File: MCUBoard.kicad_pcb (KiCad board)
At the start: 2 copper layers, 90 x 90 mm, 61 parts, among them J1 USB_B_Micro, J2 Conn_01x04, J3 Conn_02x03_Odd_Even, J4 Conn_02x05_Odd_Even, J5 Conn_01x04, J6 Conn_01x04, J7 Conn_01x16, J8 Conn_02x16_Odd_Even, J9 Conn_01x04, Q1 BSS138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

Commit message: change PB headers and route tracks for port B
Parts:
- added J10: Conn_01x04, Connector_PinHeader_2.54mm:PinHeader_1x04_P2.54mm_Vertical, F.Cu at (93.0, 86.3)
- J8: value Conn_02x16_Odd_Even -> Conn_01x18; footprint Connector_PinHeader_2.54mm:PinHeader_2x16_P2.54mm_Vertical -> Connector_PinHeader_2.54mm:PinHeader_1x18_P2.54mm_Vertical
- moved J8 36.9 mm to (137.7, 79.4), turned to 0 degrees
- moved R15 32.5 mm to (128.6, 135.9)
- moved R14 28.1 mm to (123.9, 132.3)
- moved R13 17.6 mm to (111.7, 115.2)
- moved R12 16.4 mm to (110.5, 110.2)
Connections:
- J8 pad 10: /LV0 -> /PB9
- J8 pad 11: /PB5 -> /PB10
- J8 pad 12: /LV1 -> /PB11
- J8 pad 13: /PB6 -> /PB12
- J8 pad 14: /LV2 -> /PB13
- J8 pad 15: /PB7 -> /PB14
- J8 pad 16: /LV3 -> /PB15
- J8 pad 17: /PB8 -> /PD0
- J8 pad 18: Net-(J8-Pad18) -> /PD1
- J8 pad 2: /PD0 -> /PB1
- J8 pad 3: /PB1 -> /BOOT1
- J8 pad 4: /PD1 -> /PB3
- J8 pad 5: /BOOT1 -> /PB4
- J8 pad 6: Net-(J8-Pad6) -> /PB5
- J8 pad 7: /PB3 -> /PB6
- J8 pad 8: Net-(J8-Pad8) -> /PB7
- J8 pad 9: /PB4 -> /PB8
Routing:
- net /PB15: track 0.00 -> 27.1 mm
- net /PB8: track 0.00 -> 25.8 mm, vias 0 -> 2
- net /PB14: track 0.00 -> 25.0 mm
- net /PB11: track 0.00 -> 24.2 mm, vias 0 -> 2
- net /PB0: track 0.00 -> 24.2 mm
- net /PB10: track 0.00 -> 24.0 mm, vias 0 -> 2
- net /PB4: track 0.00 -> 23.1 mm, vias 0 -> 2
- net /PB3: track 0.00 -> 23.0 mm, vias 0 -> 2
- net /PB13: track 0.00 -> 23.0 mm
- net /PB7: track 0.00 -> 22.9 mm, vias 0 -> 2
- net /PB1: track 0.00 -> 22.6 mm
- net /PB6: track 0.00 -> 22.6 mm, vias 0 -> 2
- net /PB9: track 0.00 -> 22.6 mm, vias 0 -> 2
- net /PB5: track 0.00 -> 22.4 mm, vias 0 -> 2
- net /PB12: track 0.00 -> 20.9 mm
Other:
- net class Default: clearance 0.2 -> 0.155; trace_width 0.25 -> 0.155; via_dia 0.8 -> 0.6; via_drill 0.4 -> 0.3
- net class six mil added: clearance 0.155, trace_width 0.155, via_dia 0.8, via_drill 0.4
- rule trace_clearance: 0.2 -> 0.155
- rule trace_min: 0.2 -> 0.155

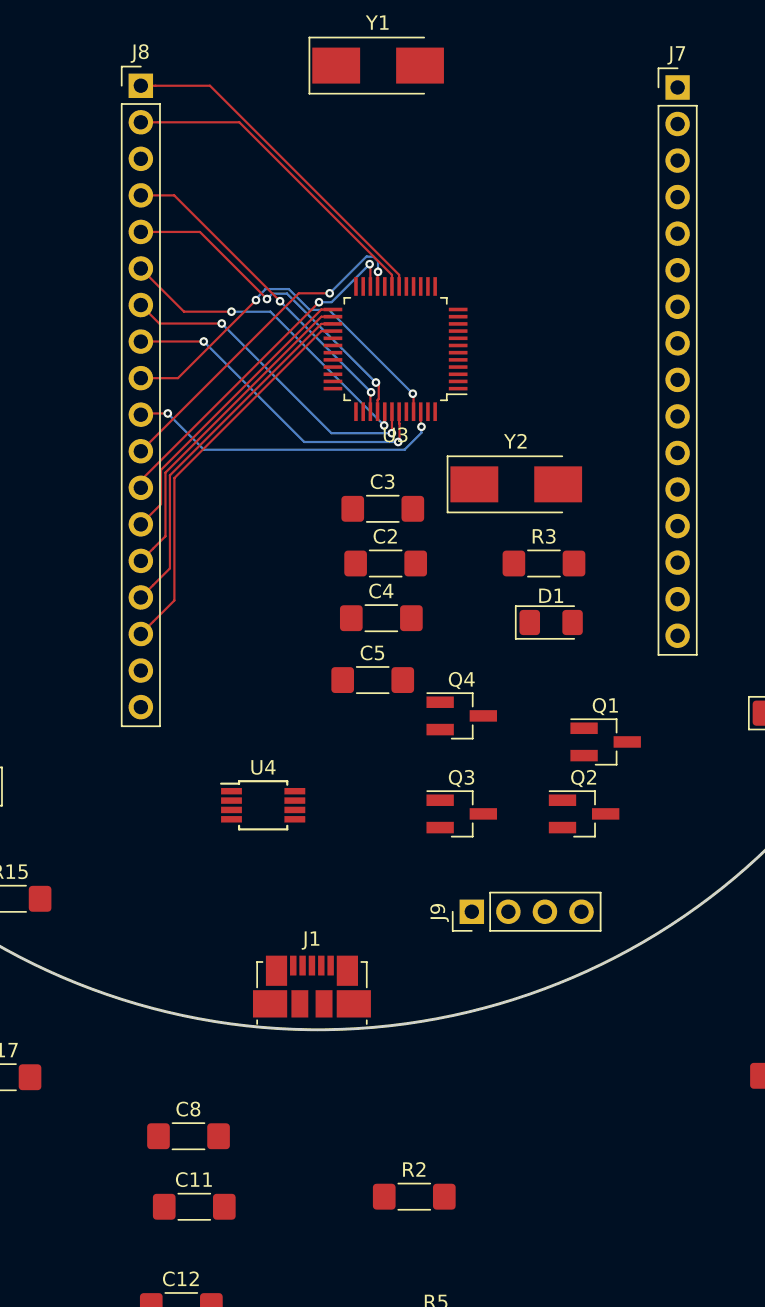
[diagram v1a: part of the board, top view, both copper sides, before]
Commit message: route portA and usb
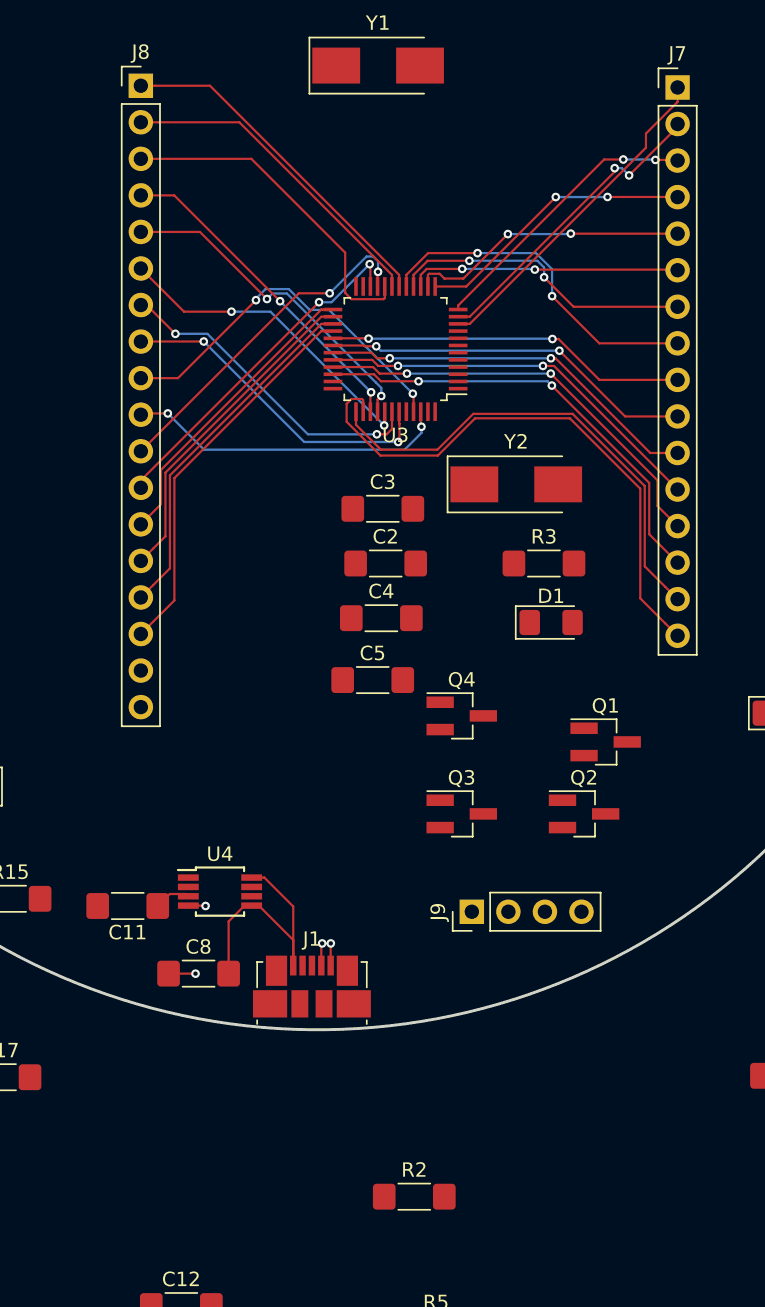
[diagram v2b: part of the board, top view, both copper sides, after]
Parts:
- moved C11 21.4 mm to (136.8, 136.4), turned to 180 degrees
- moved C8 11.3 mm to (141.7, 141.1)
- moved U4 6.71 mm to (143.2, 135.4)
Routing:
- net /PA15: track 0.00 -> 39.1 mm
- net /SWDCLK: track 0.00 -> 33.6 mm
- net /SWDIO: track 0.00 -> 31.5 mm, vias 0 -> 2
- net /PA12: track 0.00 -> 29.6 mm, vias 0 -> 2
- net /PA11: track 0.00 -> 27.7 mm, vias 0 -> 2
- net /PA10: track 0.00 -> 26.8 mm, vias 0 -> 2
- net /PA9: track 0.00 -> 26.0 mm, vias 0 -> 2
- net /PA8: track 0.00 -> 25.1 mm, vias 0 -> 2
- net /PA7: track 0.00 -> 24.0 mm, vias 0 -> 2
- net /BOOT1: track 0.00 -> 23.5 mm
- net /PA0: track 0.00 -> 23.2 mm
- net /PA1: track 0.00 -> 21.5 mm, vias 0 -> 2
- net /PA6: track 0.00 -> 21.3 mm, vias 0 -> 2
- net /PA2: track 0.00 -> 19.8 mm, vias 0 -> 2
- net /PA4: track 0.00 -> 19.6 mm, vias 0 -> 2
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
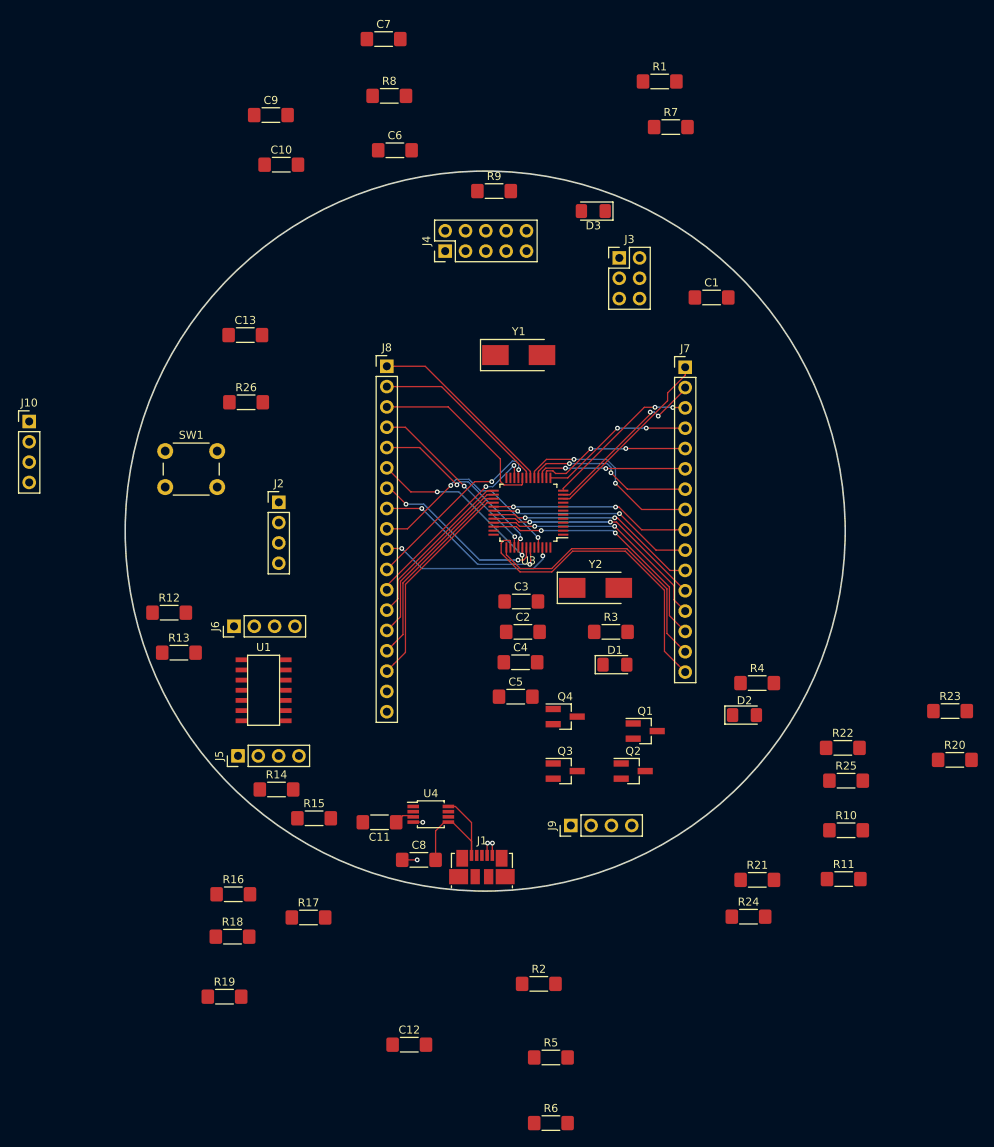
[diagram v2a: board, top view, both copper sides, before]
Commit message: routing bi-directional level shifters
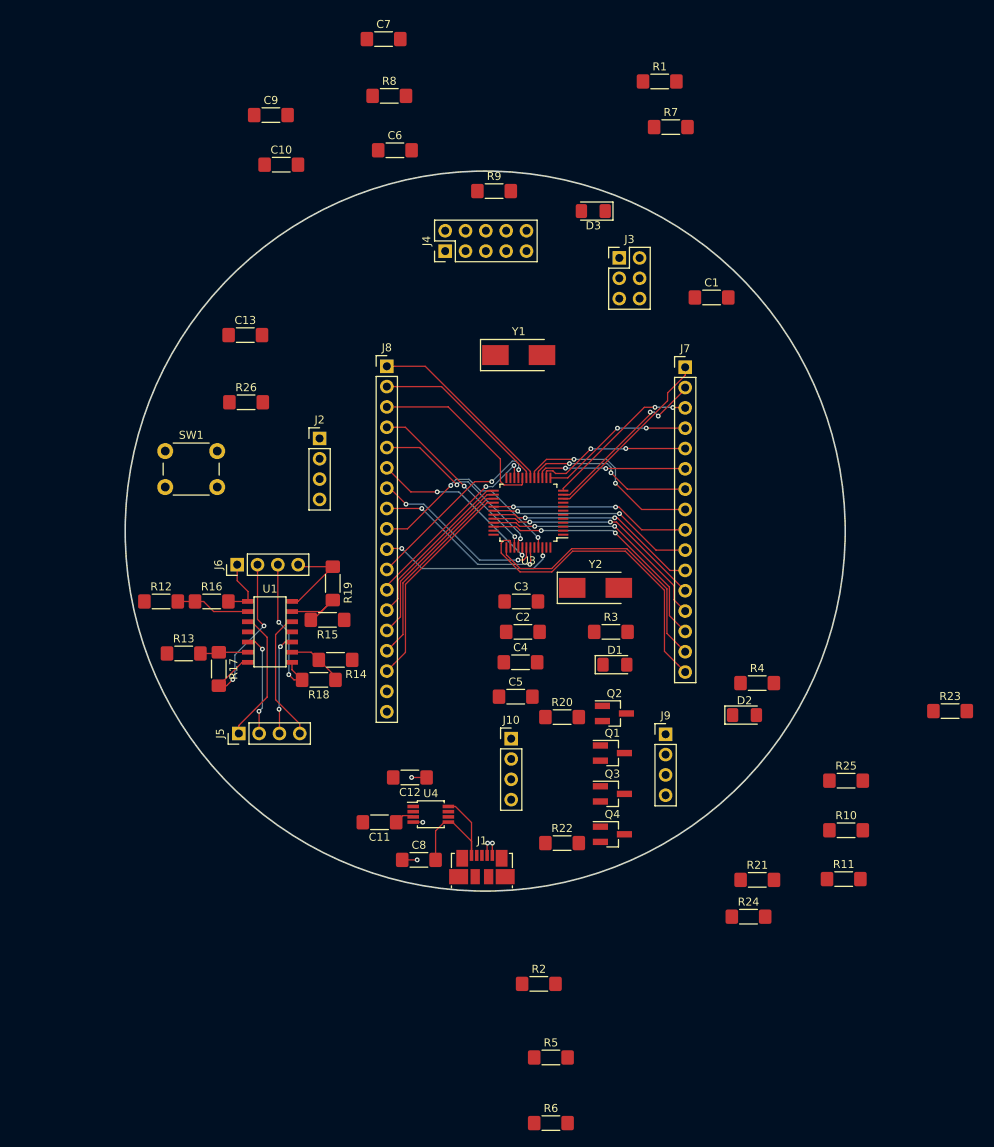
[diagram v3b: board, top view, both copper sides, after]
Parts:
- moved J10 72.1 mm to (153.2, 126.0)
- moved R19 53.4 mm to (130.9, 106.5), turned to 90 degrees
- moved R20 49.4 mm to (159.6, 123.2)
- moved R22 37.1 mm to (159.6, 139.0)
- moved R16 36.7 mm to (115.8, 108.8)
- moved R18 33.9 mm to (129.2, 118.6), turned to 180 degrees
- moved C12 33.4 mm to (140.6, 130.8), turned to 180 degrees
- moved R17 33.0 mm to (116.7, 117.2), turned to 270 degrees
- moved R15 24.9 mm to (130.3, 111.1), turned to 180 degrees
- moved R14 17.8 mm to (131.3, 116.1), turned to 180 degrees
- moved J9 16.4 mm to (172.6, 125.4), turned to 0 degrees
- moved Q4 15.8 mm to (165.9, 137.9)
- moved J2 9.47 mm to (129.3, 88.4)
- moved J6 7.71 mm to (119.0, 104.2)
- moved Q2 7.57 mm to (166.2, 122.8)
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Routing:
- net Net-(J6-Pad2): track 0.00 -> 23.2 mm, vias 0 -> 2
- net Net-(J6-Pad3): track 0.00 -> 19.0 mm, vias 0 -> 2
- net Net-(J5-Pad1): track 0.00 -> 16.7 mm
- net Net-(J5-Pad4): track 0.00 -> 16.3 mm
- net Net-(J5-Pad2): track 0.00 -> 12.9 mm, vias 0 -> 2
- net Net-(J5-Pad3): track 0.00 -> 12.6 mm, vias 0 -> 2
- net Net-(J6-Pad4): track 0.00 -> 11.3 mm
- net Net-(R15-Pad2): track 0.00 -> 9.47 mm
- net Net-(R12-Pad2): track 0.00 -> 9.30 mm
- net Net-(J6-Pad1): track 0.00 -> 7.60 mm
- net Net-(R14-Pad2): track 0.00 -> 7.11 mm
- net Net-(R13-Pad2): track 0.00 -> 6.02 mm
- net GND: track 6.19 -> 8.07 mm, vias 4 -> 5

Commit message: route all non-power tracks
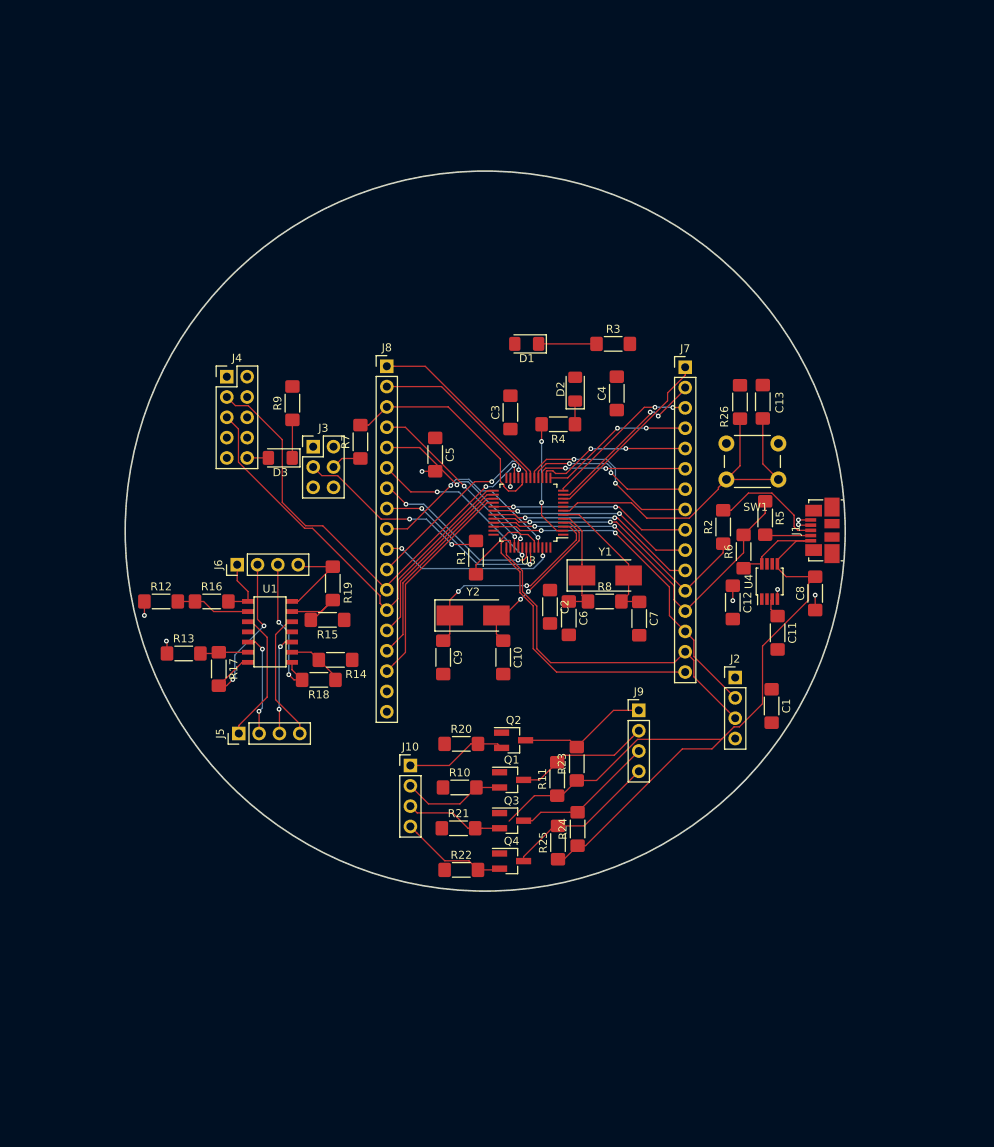
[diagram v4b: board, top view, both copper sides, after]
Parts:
- moved C7 79.2 mm to (169.2, 110.9), turned to 270 degrees
- moved R6 75.4 mm to (182.3, 102.6), turned to 90 degrees
- moved R5 72.6 mm to (185.0, 98.4), turned to 270 degrees
- moved C9 71.1 mm to (144.8, 115.8), turned to 270 degrees
- moved SW1 70.2 mm to (180.2, 89.0)
- moved R8 68.7 mm to (164.9, 108.8)
- moved C10 67.5 mm to (152.2, 115.8), turned to 270 degrees
- moved C13 65.2 mm to (184.7, 83.8), turned to 90 degrees
- moved R1 63.8 mm to (148.8, 103.3), turned to 90 degrees
- moved C6 62.4 mm to (160.4, 110.9), turned to 270 degrees
- moved R26 61.7 mm to (181.8, 83.9), turned to 270 degrees
- moved R2 61.6 mm to (179.8, 99.5), turned to 90 degrees
- moved J2 59.9 mm to (181.2, 118.3)
- moved J1 59.9 mm to (192.2, 99.9), turned to 90 degrees
- moved C8 59.7 mm to (191.2, 107.8), turned to 90 degrees
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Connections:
- C11 pad 2: /VCC3V3 -> Net-(C11-Pad2)
- C12 pad 2: /VCC3V3 -> Net-(C11-Pad2)
- C6 pad 1: /OSCIN -> /PD0
- C6 pad 2: Net-(C6-Pad2) -> GND
- C7 pad 1: /OSCOUT -> /PD1
- C7 pad 2: Net-(C6-Pad2) -> GND
- J10 pad 1: Net-(J10-Pad1) -> /LV0
- J10 pad 2: Net-(J10-Pad2) -> /LV1
- J10 pad 3: Net-(J10-Pad3) -> /LV2
- J10 pad 4: Net-(J10-Pad4) -> /LV3
- J8 pad 17: /PD0 -> GND
- J8 pad 18: /PD1 -> GND
- Q1 pad 1: /VCC3V3 -> +3V3
- Q2 pad 1: /VCC3V3 -> +3V3
- Q3 pad 1: /VCC3V3 -> +3V3
- Q4 pad 1: /VCC3V3 -> +3V3
- R10 pad 1: /VCC3V3 -> +3V3
- R20 pad 1: /VCC3V3 -> +3V3
- R21 pad 1: /VCC3V3 -> +3V3
- R22 pad 1: /VCC3V3 -> +3V3
- R8 pad 1: /OSCIN -> /PD0
- R8 pad 2: /OSCOUT -> /PD1
- U3 pad 1: /VCC3V3 -> +3V3
- U3 pad 24: /VCC3V3 -> +3V3
- U3 pad 36: /VCC3V3 -> +3V3
- U3 pad 48: /VCC3V3 -> +3V3
- U3 pad 9: /VCC3V3 -> +3V3
- U4 pad 1: /VCC3V3 -> Net-(C11-Pad2)
- U4 pad 2: /VCC3V3 -> Net-(C11-Pad2)
- Y1 pad 1: /OSCIN -> /PD0
- Y1 pad 2: /OSCOUT -> /PD1
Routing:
- net +5V: track 19.2 -> 104.7 mm
- net /NRST: track 0.00 -> 47.0 mm
- net /PB11: track 24.2 -> 58.8 mm
- net /PB12: track 20.9 -> 53.9 mm
- net /PC14: track 0.00 -> 27.2 mm, vias 0 -> 2
- net Net-(J3-Pad3): track 0.00 -> 24.5 mm, vias 0 -> 2
- net /PC15: track 0.00 -> 21.3 mm, vias 0 -> 2
- net Net-(J9-Pad4): track 0.00 -> 19.4 mm
- net /PD1: track 0.00 -> 18.0 mm
- net Net-(J9-Pad3): track 0.00 -> 18.0 mm
- net /PA12: track 29.6 -> 47.4 mm
- net Net-(J9-Pad2): track 0.00 -> 16.9 mm
- net Net-(J9-Pad1): track 0.00 -> 16.4 mm
- net /PC13: track 0.00 -> 14.9 mm, vias 0 -> 2
- net Net-(J1-Pad3): track 0.00 -> 14.6 mm
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
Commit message: board routed
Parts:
- moved C2 10.4 mm to (156.4, 119.8)
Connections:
- C11 pad 2: Net-(C11-Pad2) -> +3V3
- C12 pad 2: Net-(C11-Pad2) -> +3V3
- U4 pad 1: Net-(C11-Pad2) -> +3V3
- U4 pad 2: Net-(C11-Pad2) -> +3V3
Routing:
- net +3V3: track 0.00 -> 432.9 mm
- net GND: track 14.2 -> 427.6 mm, vias 9 -> 31
- net +5V: track 104.7 -> 214.5 mm
- net /NRST: track 47.0 -> 45.8 mm, vias 0 -> 2
- net /SWDIO: track 42.4 -> 43.1 mm
- net /PA11: track 35.5 -> 36.2 mm, vias 2 -> 4
- net /PA12: track 47.4 -> 47.5 mm, vias 2 -> 4
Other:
- board text added: "MCUBoard"
